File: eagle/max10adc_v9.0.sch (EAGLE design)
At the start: 198 parts, among them IC1 MAX19506, IC2 MAX19506, J1 MOLEX_BNC_73100-0105, J2 MOLEX_BNC_73100-0105, J3 MOLEX_BNC_73100-0105, J4 MOLEX_BNC_73100-0105, K1 AQY21SOP, K2 AQY21SOP, K3 AQY21SOP, K4 AQY21SOP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

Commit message: clean up a few things
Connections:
- net N$20 renamed NSG_1
- net N$24 renamed N10M_1
- net N$29 renamed N50_1
- net N$37 renamed NNG_1
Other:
- moved on the sheet: C_OSC, OSC, PIN_LEFT

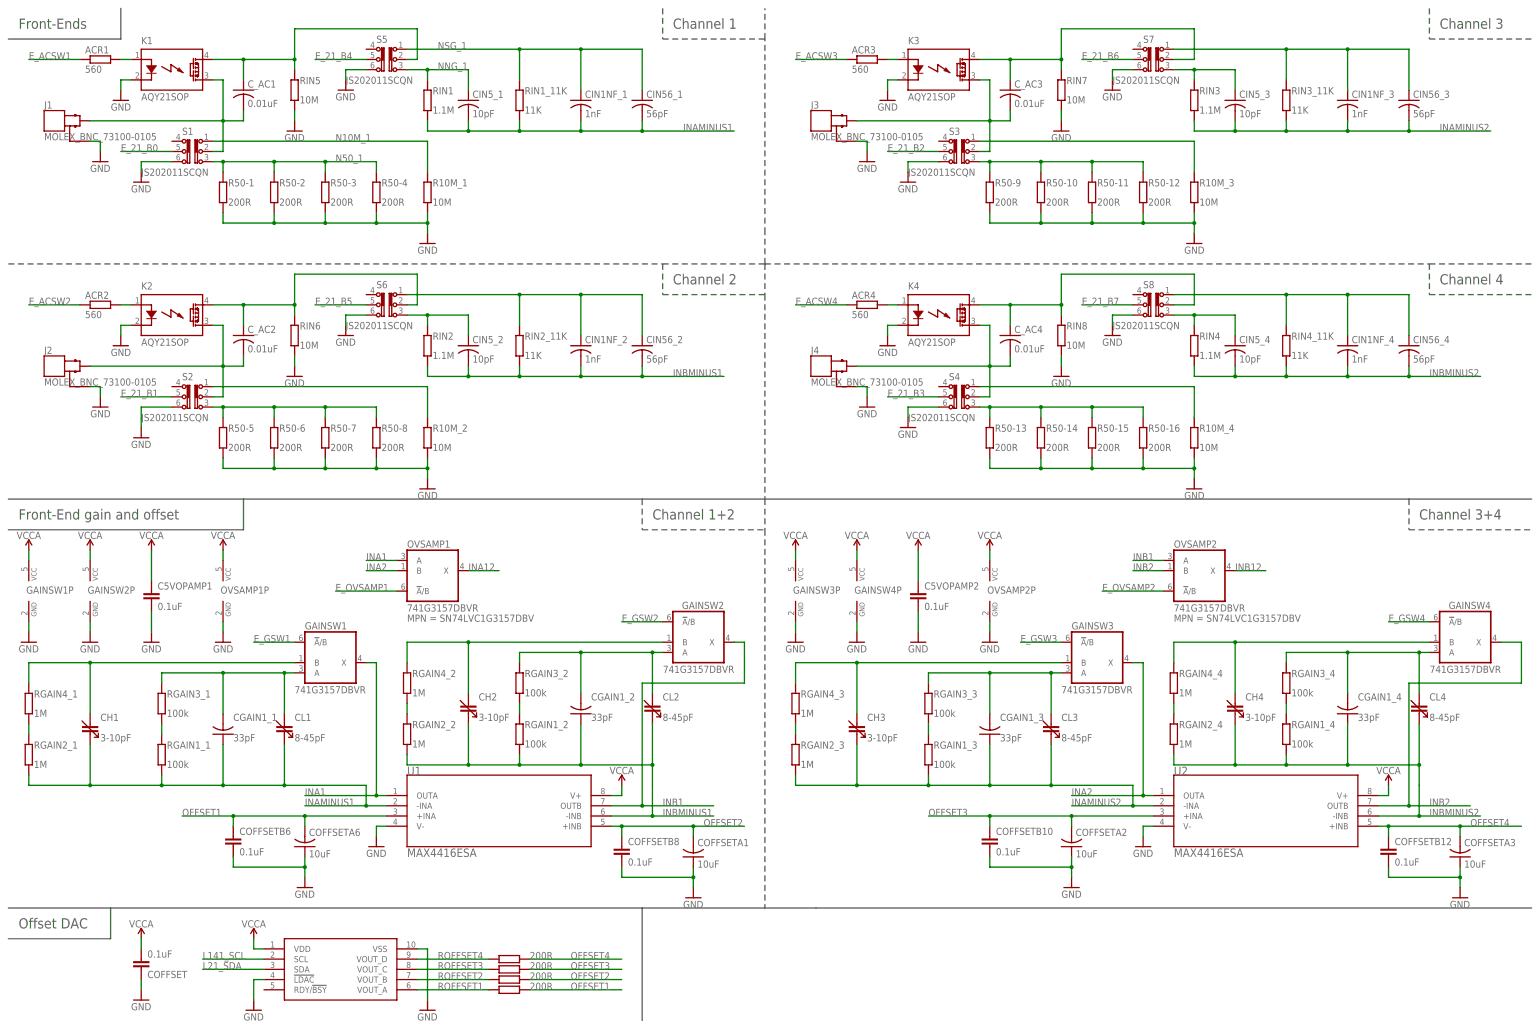
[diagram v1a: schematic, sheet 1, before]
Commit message: add some notes to the schematics
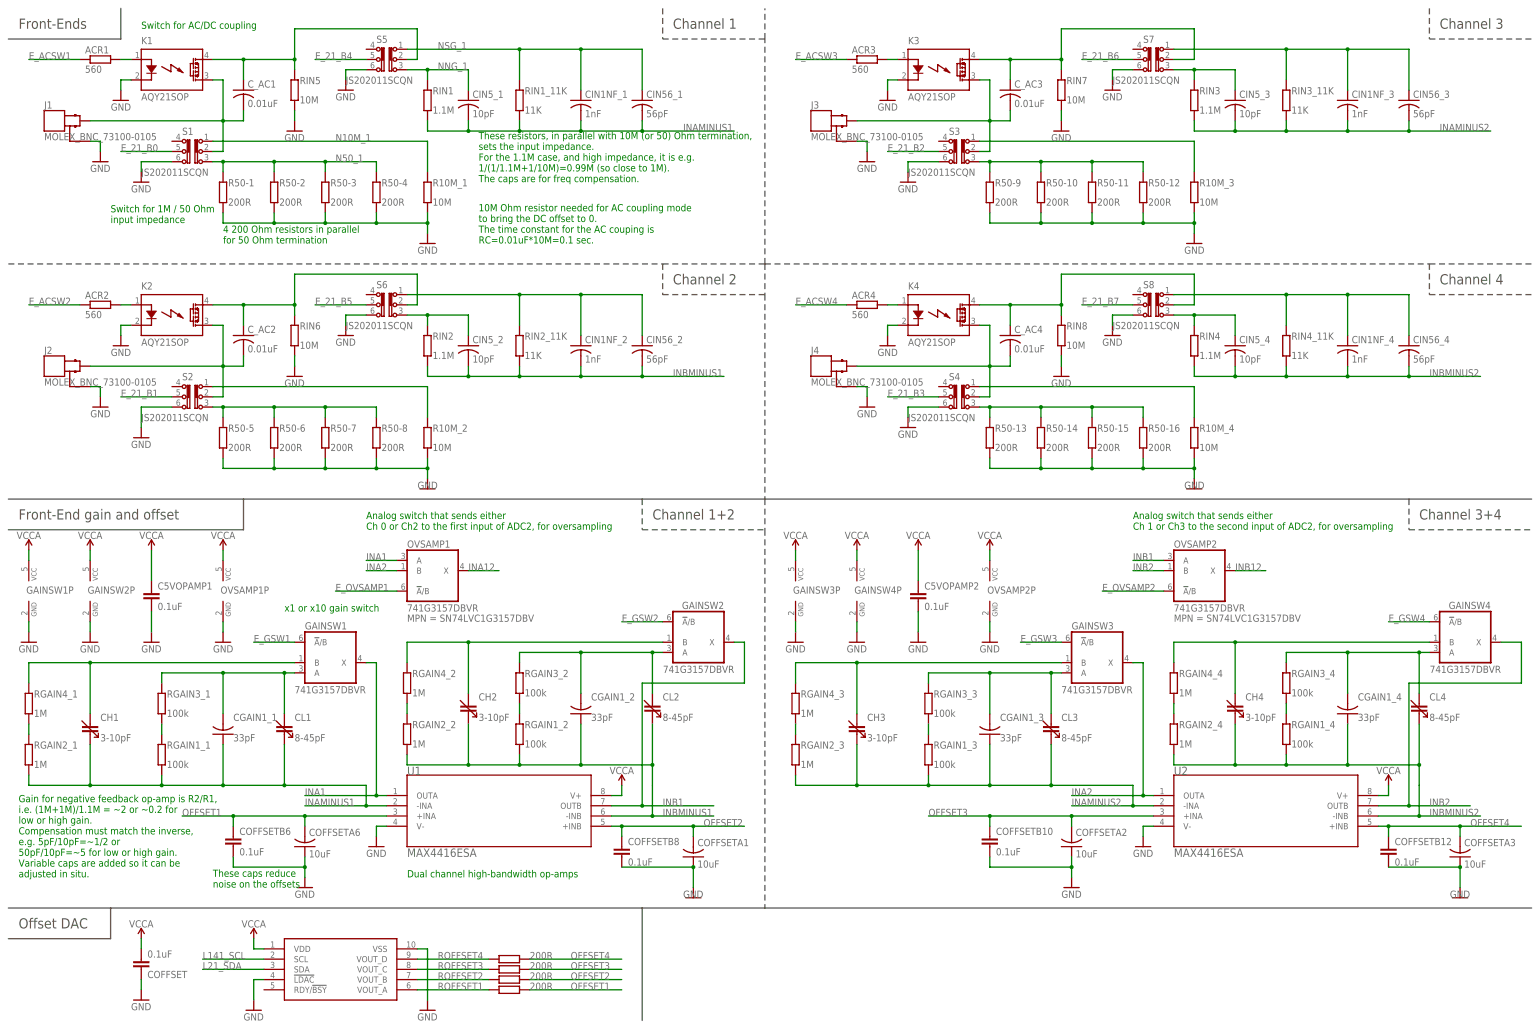
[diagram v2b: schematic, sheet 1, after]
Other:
- note added: "10M Ohm resistor needed for AC coupling mode to bring the DC offset to 0. The time constant for the AC couping is RC=0.01uF*10M=0.1 sec."
- note added: "4 200 Ohm resistors in parallel for 50 Ohm termination"
- note added: "Analog switch that sends either Ch 0 or Ch2 to the first input of ADC2, for oversampling"
- note added: "Analog switch that sends either Ch 1 or Ch3 to the second input of ADC2, for oversampling"
- note added: "Can take 5V from either the right side connector or the USB connector"
- note added: "Chip that talks UART over USB"
- note added: "Dual 8-bit ADC outputs"
- note added: "Dual channel high-bandwidth op-amps"
- note added: "For reducing noise on the power. The inductor helps reduce low-freq noise on the USB 5V power input."
- note added: "Gain for negative feedback op-amp is R2/R1, i.e. (1M+1M)/1.1M = ~2 or ~0.2 for low or high gain. Compensation must match the inverse, e.g. 5pF/10pF=~1/2 or 50pF/10pF=~5 for low or high gain. Variable caps are added so it can be adjusted in situ."
- note added: "Inputs to this ADC are from the oversampling switches"
- note added: "Note that the two ADCs have separate clocks (32 and 33), which can be 50% out of phase, for oversampling."
- note added: "SDIN/SCLK,CS is the SPI interface"
- note added: "SHDN is used to turn off the ADCs when inactive, to save power"
- note added: "Separate 3.3V power rail for the analog components, so noise from FPGA etc. doesn't get into ADCs."
- note added: "Switch for 1M / 50 Ohm input impedance"
- note added: "Switch for AC/DC coupling"
- note added: "These caps reduce noise on the offsets"
- note added: "These resistors, in parallel with 10M (or 50) Ohm termination, sets the input impedance. For the 1.1M case, and high impedance, it is e.g. 1/(1/1.1M+1/10M)=0.99M (so close to 1M). The caps are for freq compensation."
- note added: "x1 or x10 gain switch"
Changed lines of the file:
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@@
 <wire x1="5.08" y1="193.04" x2="167.64" y2="193.04" width="0.1524" layer="97" style="shortdash"/>
 <wire x1="167.64" y1="193.04" x2="193.04" y2="193.04" width="0.1524" layer="97" style="shortdash"/>
-<wire x1="193.04" y1="193.04" x2="193.04" y2="200.66" width="0.1524" layer="97" style="shortdash"/>
-<wire x1="193.04" y1="200.66" x2="193.04" y2="248.92" width="0.1524" layer="97" style="shortdash"/>
+<wire x1="193.04" y1="193.04" x2="193.04" y2="248.92" width="0.1524" layer="97" style="shortdash"/>
 <wire x1="193.04" y1="248.92" x2="193.04" y2="256.54" width="0.1524" layer="97" style="shortdash"/>
 <wire x1="193.04" y1="193.04" x2="358.14" y2="193.04" width="0.1524" layer="97" style="shortdash"/>
@@
 <wire x1="30.48" y1="33.02" x2="162.56" y2="33.02" width="0.1524" layer="97"/>
 <wire x1="162.56" y1="33.02" x2="193.04" y2="33.02" width="0.1524" layer="97"/>
-<wire x1="193.04" y1="33.02" x2="205.74" y2="33.02" width="0.1524" layer="97"/>
-<wire x1="205.74" y1="33.02" x2="383.54" y2="33.02" width="0.1524" layer="97"/>
+<wire x1="193.04" y1="33.02" x2="383.54" y2="33.02" width="0.1524" layer="97"/>
 <wire x1="193.04" y1="134.62" x2="193.04" y2="127" width="0.1524" layer="97" style="shortdash"/>
 <wire x1="193.04" y1="127" x2="193.04" y2="33.02" width="0.1524" layer="97" style="shortdash"/>
@@
 <wire x1="30.48" y1="25.4" x2="30.48" y2="33.02" width="0.1524" layer="97"/>
 <wire x1="162.56" y1="33.02" x2="162.56" y2="5.08" width="0.1524" layer="97"/>
+<text x="58.42" y="198.12" size="1.778" layer="91">4 200 Ohm resistors in parallel
+for 50 Ohm termination</text>
+<text x="121.92" y="198.12" size="1.778" layer="91">10M Ohm resistor needed for AC coupling mode
+to bring the DC offset to 0.
+The time constant for the AC couping is
+RC=0.01uF*10M=0.1 sec.</text>
+<text x="121.92" y="213.36" size="1.778" layer="91">These resistors, in parallel with 10M (or 50) Ohm termination,
+sets the input impedance.
+For the 1.1M case, and high impedance, it is e.g.
+1/(1/1.1M+1/10M)=0.99M (so close to 1M).
+The caps are for freq compensation.</text>
+<text x="38.1" y="251.46" size="1.778" layer="91">Switch for AC/DC coupling</text>
+<text x="30.48" y="203.2" size="1.778" layer="91">Switch for 1M / 50 Ohm
+input impedance</text>
+<text x="93.98" y="127" size="1.778" layer="91">Analog switch that sends either
+Ch 0 or Ch2 to the first input of ADC2, for oversampling</text>
+<text x="284.48" y="127" size="1.778" layer="91">Analog switch that sends either
+Ch 1 or Ch3 to the second input of ADC2, for oversampling</text>
+<text x="104.14" y="40.64" size="1.778" layer="91">Dual channel high-bandwidth op-amps</text>
+<text x="73.66" y="106.68" size="1.778" layer="91">x1 or x10 gain switch</text>
+<text x="55.88" y="38.1" size="1.778" layer="91">These caps reduce
+noise on the offsets</text>
+<text x="7.62" y="40.64" size="1.778" layer="91">Gain for negative feedback op-amp is R2/R1,
+i.e. (1M+1M)/1.1M = ~2 or ~0.2 for
+low or high gain.
+Compensation must match the inverse,
+e.g. 5pF/10pF=~1/2 or
+50pF/10pF=~5 for low or high gain.
+Variable caps are added so it can be
+adjusted in situ.</text>
 </plain>
 <instances>
@@
 </instance>
 <instance part="GND59" gate="1" x="175.26" y="35.56">
-<attribute name="VALUE" x="172.72" y="33.02" size="1.778" layer="96"/>
+<attribute name="VALUE" x="172.72" y="35.56" size="1.778" layer="96"/>
 </instance>
 <instance part="COFFSETB10" gate="G$1" x="248.92" y="48.26" rot="MR180">
@@
 </instance>
 <instance part="GND73" gate="1" x="109.22" y="137.16" rot="MR0">
-<attribute name="VALUE" x="111.76" y="134.62" size="1.778" layer="96" rot="MR0"/>
+<attribute name="VALUE" x="111.76" y="137.16" size="1.778" layer="96" rot="MR0"/>
 </instance>
 <instance part="GND74" gate="1" x="33.02" y="172.72" rot="MR0">
@@
 </instance>
 <instance part="GND31" gate="1" x="299.72" y="137.16" rot="MR0">
-<attribute name="VALUE" x="302.26" y="134.62" size="1.778" layer="96" rot="MR0"/>
+<attribute name="VALUE" x="302.26" y="137.16" size="1.778" layer="96" rot="MR0"/>
 </instance>
 <instance part="GND56" gate="1" x="223.52" y="172.72" rot="MR0">
@@
 </instance>
 <instance part="GND57" gate="1" x="365.76" y="35.56">
-<attribute name="VALUE" x="363.22" y="33.02" size="1.778" layer="96"/>
+<attribute name="VALUE" x="363.22" y="35.56" size="1.778" layer="96"/>
 </instance>
 <instance part="U$16" gate="G$1" x="347.98" y="63.5">
@@
 <pinref part="GND59" gate="1" pin="GND"/>
 <pinref part="COFFSETA1" gate="G$1" pin="1"/>
-<wire x1="175.26" y1="38.1" x2="175.26" y2="40.64" width="0.1524" layer="91"/>
+<wire x1="175.26" y1="38.1" x2="175.26" y2="43.18" width="0.1524" layer="91"/>
 <pinref part="COFFSETB8" gate="G$1" pin="1"/>
-<wire x1="175.26" y1="40.64" x2="175.26" y2="43.18" width="0.1524" layer="91"/>
-<wire x1="157.48" y1="43.18" x2="157.48" y2="40.64" width="0.1524" layer="91"/>
-<wire x1="157.48" y1="40.64" x2="175.26" y2="40.64" width="0.1524" layer="91"/>
-<junction x="175.26" y="40.64"/>
+<wire x1="157.48" y1="43.18" x2="175.26" y2="43.18" width="0.1524" layer="91"/>
+<junction x="175.26" y="43.18"/>
 </segment>
 <segment>
@@
 <segment>
 <pinref part="GND57" gate="1" pin="GND"/>
-<wire x1="365.76" y1="38.1" x2="365.76" y2="40.64" width="0.1524" layer="91"/>
-<wire x1="365.76" y1="40.64" x2="365.76" y2="43.18" width="0.1524" layer="91"/>
-<wire x1="347.98" y1="43.18" x2="347.98" y2="40.64" width="0.1524" layer="91"/>
-<wire x1="347.98" y1="40.64" x2="365.76" y2="40.64" width="0.1524" layer="91"/>
-<junction x="365.76" y="40.64"/>
+<wire x1="365.76" y1="38.1" x2="365.76" y2="43.18" width="0.1524" layer="91"/>
+<wire x1="347.98" y1="43.18" x2="365.76" y2="43.18" width="0.1524" layer="91"/>
+<junction x="365.76" y="43.18"/>
 <pinref part="COFFSETA3" gate="G$1" pin="1"/>
 <pinref part="COFFSETB12" gate="G$1" pin="1"/>
@@
 <wire x1="304.8" y1="203.2" x2="292.1" y2="203.2" width="0.1524" layer="97"/>
 <wire x1="335.28" y1="157.48" x2="292.1" y2="157.48" width="0.1524" layer="97"/>
+<text x="243.84" y="35.56" size="1.778" layer="91">Can take 5V from either the
+right side connector
+or the USB connector</text>
+<text x="335.28" y="30.48" size="1.778" layer="91">Chip that talks UART
+over USB</text>
 </plain>
 <instances>
@@
 <plain>
 <wire x1="218.44" y1="256.54" x2="218.44" y2="132.08" width="0.1524" layer="95"/>
-<wire x1="218.44" y1="132.08" x2="5.08" y2="132.08" width="0.1524" layer="95"/>
+<wire x1="218.44" y1="132.08" x2="119.38" y2="132.08" width="0.1524" layer="95"/>
 <text x="7.62" y="251.46" size="2.54" layer="95">ADCs</text>
 <wire x1="5.08" y1="248.92" x2="17.78" y2="248.92" width="0.1524" layer="97"/>
@@
 <wire x1="106.68" y1="124.46" x2="106.68" y2="132.08" width="0.1524" layer="97" style="shortdash"/>
 <wire x1="109.22" y1="132.08" x2="109.22" y2="248.92" width="0.1524" layer="97" style="shortdash"/>
-<wire x1="109.22" y1="248.92" x2="109.22" y2="254" width="0.1524" layer="97" style="shortdash"/>
-<wire x1="109.22" y1="254" x2="109.22" y2="256.54" width="0.1524" layer="97" style="shortdash"/>
+<wire x1="109.22" y1="248.92" x2="109.22" y2="256.54" width="0.1524" layer="97" style="shortdash"/>
 <text x="81.28" y="251.46" size="2.54" layer="97" font="vector">Channel 1+2</text>
 <text x="193.04" y="251.46" size="2.54" layer="97" font="vector">Channel 3+4</text>
@@
 <text x="5.08" y="50.8" size="2.54" layer="97" font="vector">Misc.</text>
 <wire x1="119.38" y1="55.88" x2="119.38" y2="5.08" width="0.1524" layer="97"/>
+<text x="66.04" y="226.06" size="1.778" layer="91">Note that the two ADCs have separate
+clocks (32 and 33), which can be
+50% out of phase, for oversampling.</text>
+<text x="83.82" y="167.64" size="1.778" layer="91">SHDN is used to turn
+off the ADCs when
+inactive, to save power</text>
+<text x="86.36" y="187.96" size="1.778" layer="91">SDIN/SCLK,CS
+is the SPI interface</text>
+<text x="15.24" y="193.04" size="1.778" layer="91">Dual 8-bit
+ADC outputs</text>
+<text x="114.3" y="165.1" size="1.778" layer="91">Inputs to this ADC
+are from the
+oversampling switches</text>
+<text x="22.352" y="92.964" size="1.778" layer="91">For reducing noise on the power.
+The inductor helps reduce low-freq
+noise on the USB 5V power input.</text>
+<text x="22.352" y="57.404" size="1.778" layer="91">Separate 3.3V power rail for the
+analog components, so noise from
+FPGA etc. doesn't get into ADCs.</text>
 </plain>
 <instances>
